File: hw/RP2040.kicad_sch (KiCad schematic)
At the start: 30 parts, among them SW2 SW_Push, U5 W25Q128JVSIQ, U6 RP2040, Y1 Crystal_GND24

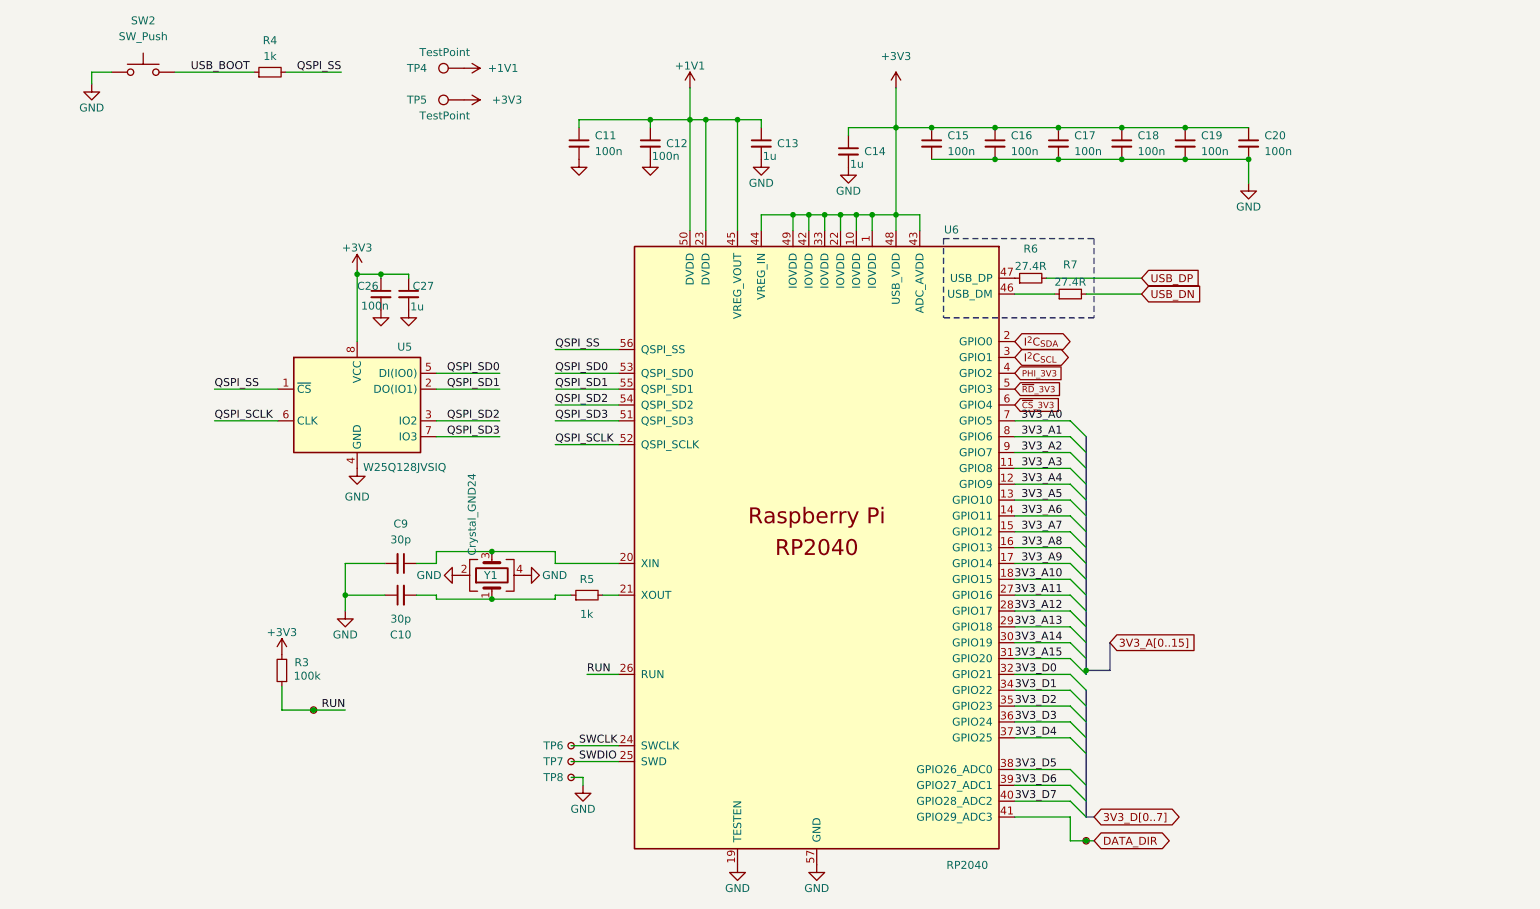
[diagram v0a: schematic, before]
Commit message: hw: use nets for decoupling capacitors
Signed-off-by: Mahyar Koshkouei <mk@deltabeard.com>
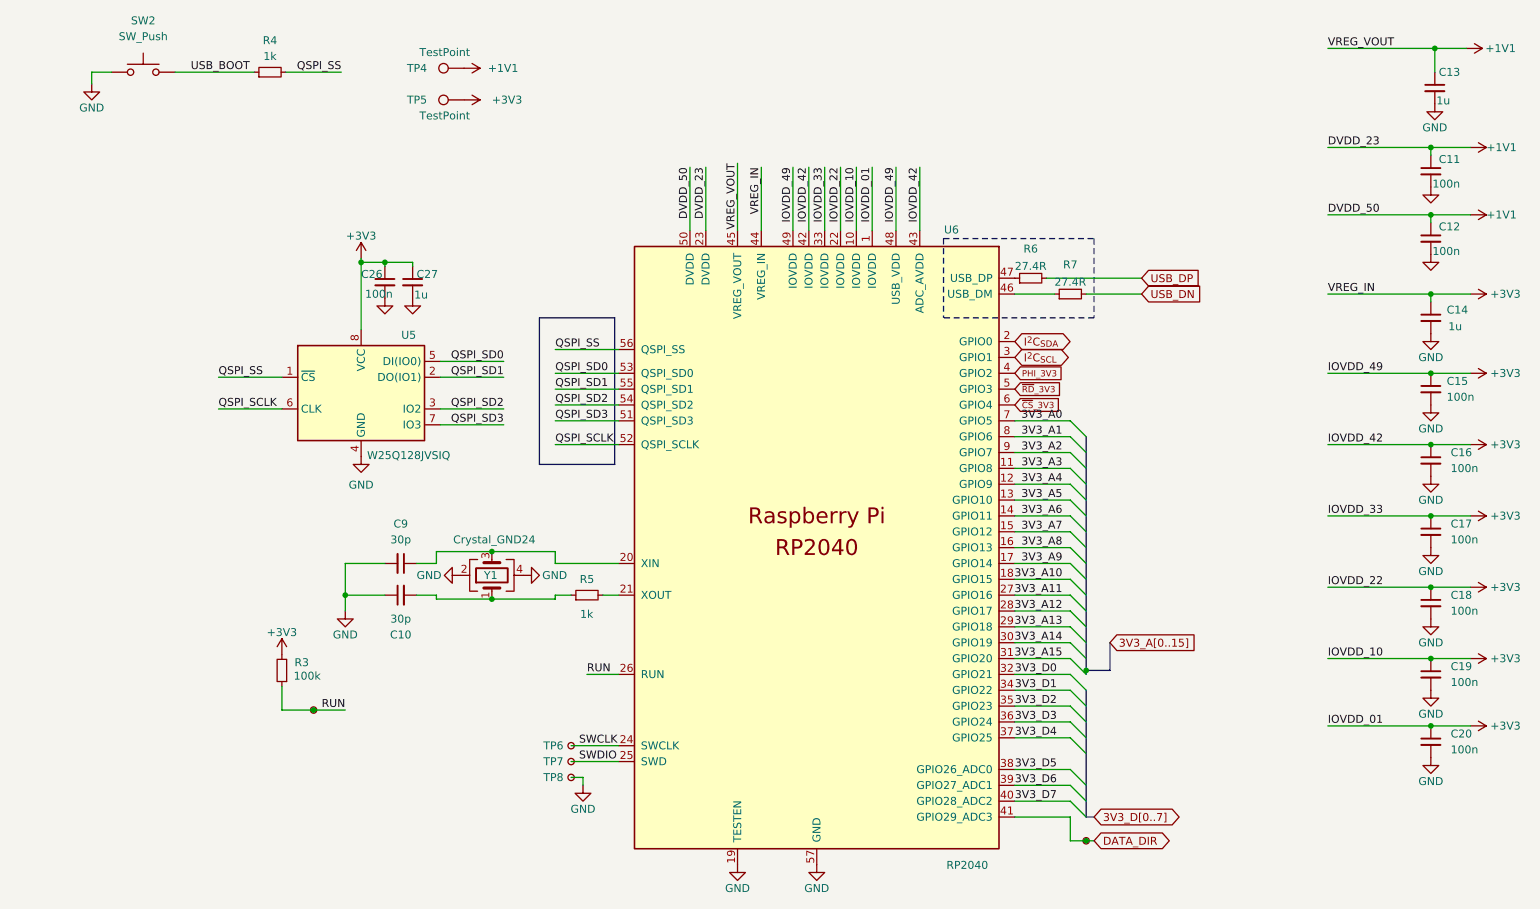
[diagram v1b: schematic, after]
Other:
- moved on the sheet: C14, C15, C26, C27, U5

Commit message: More attempts
Signed-off-by: Mahyar Koshkouei <mk@deltabeard.com>
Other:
- note added: "TODO: Internal pull-up exists on RUN pin."
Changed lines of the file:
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@@
     (stroke (width 0) (type dash) (color 0 0 0 0))
+  )
+  (text "TODO: Internal pull-up exists on RUN pin." (at 45.72 130.81 0)
+    (effects (font (size 1.27 1.27)) (justify left bottom))
   )
   (label "USB_BOOT" (at 50.8 25.4 0)

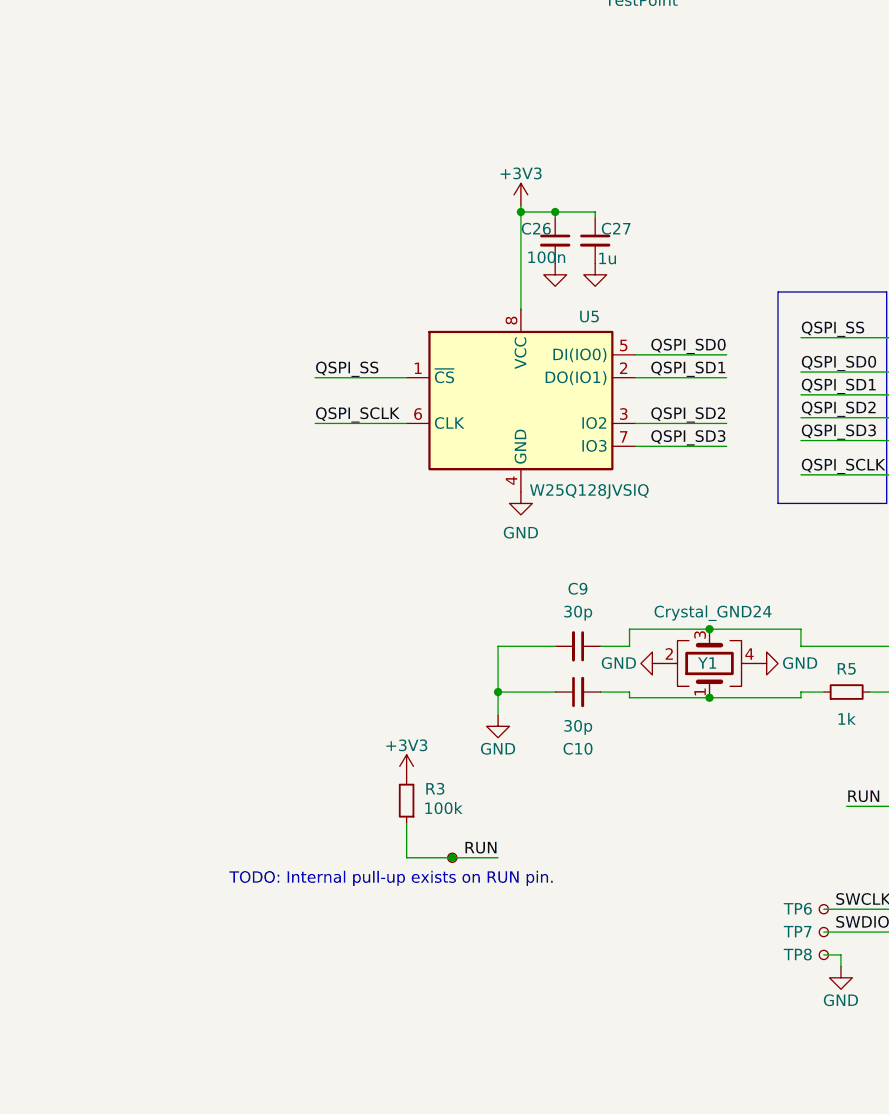
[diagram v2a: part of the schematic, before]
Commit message: hw: minor rearranging of symbols
Signed-off-by: Mahyar Koshkouei <mk@deltabeard.com>
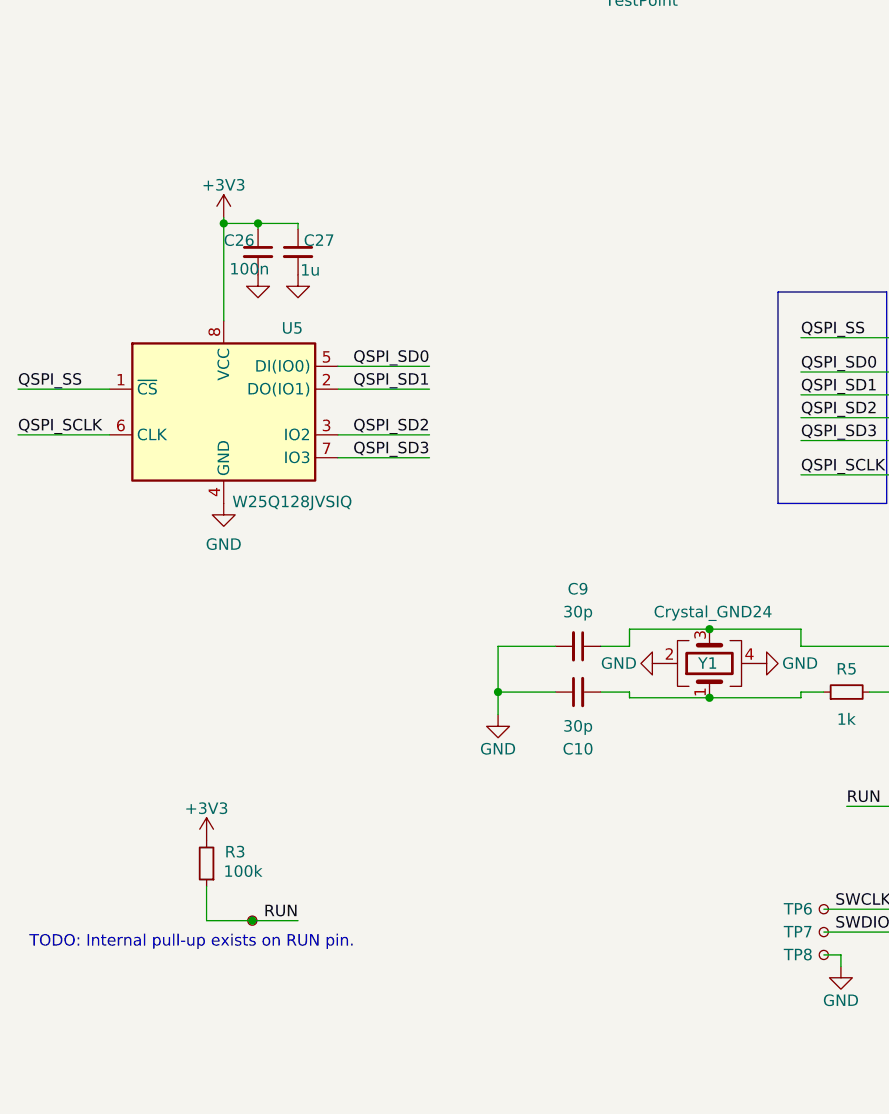
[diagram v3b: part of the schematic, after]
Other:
- moved on the sheet: C26, C27, R3, U5

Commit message: all: Add open source license
Signed-off-by: Mahyar Koshkouei <mk@deltabeard.com>
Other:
- company: Mahyar Koshkouei -> Copyright (c) 2021 Mahyar Koshkouei
- title: RP2040 Game Boy Cart -> DBGC: RP2040 Game Boy Cart
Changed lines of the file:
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@@
   (paper "A4")
   (title_block
-    (title "RP2040 Game Boy Cart")
+    (title "DBGC: RP2040 Game Boy Cart")
     (date "2021-09-29")
     (rev "0.3a")
-    (company "Mahyar Koshkouei")
-    (comment 1 "All Rights Reserved")
+    (company "Copyright (c) 2021 Mahyar Koshkouei")
+    (comment 1 "CC BY-SA 4.0")
     (comment 2 "Compatible with DMG, MGB, & CGB. Collectively referred to as \"GB\" here.")
   )
